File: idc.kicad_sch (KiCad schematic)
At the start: 3 parts, among them Q2401 MMDT5401

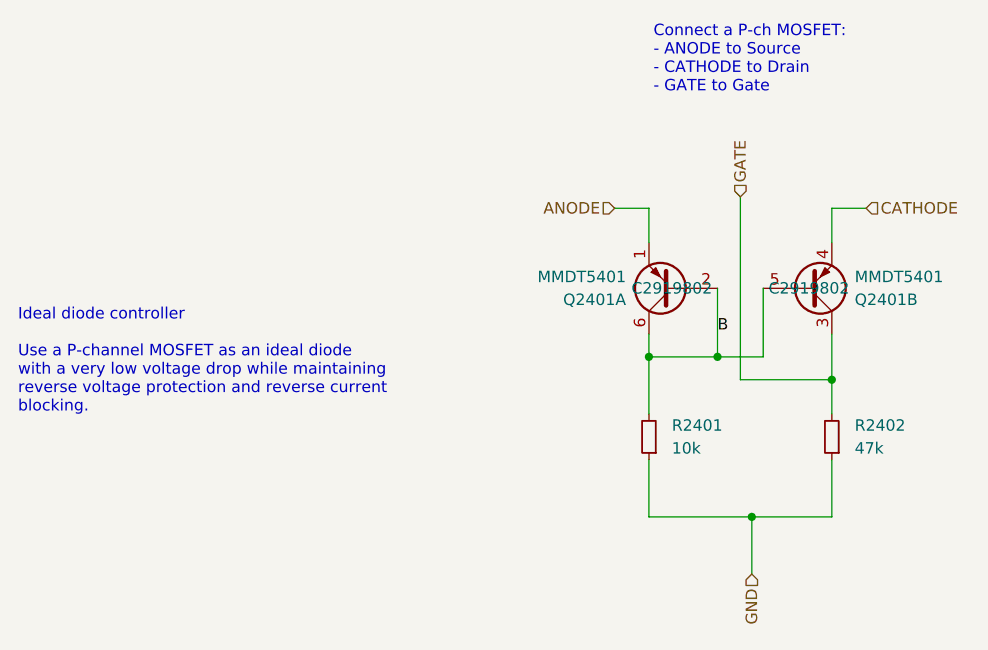
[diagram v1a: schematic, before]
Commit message: Reannotate components
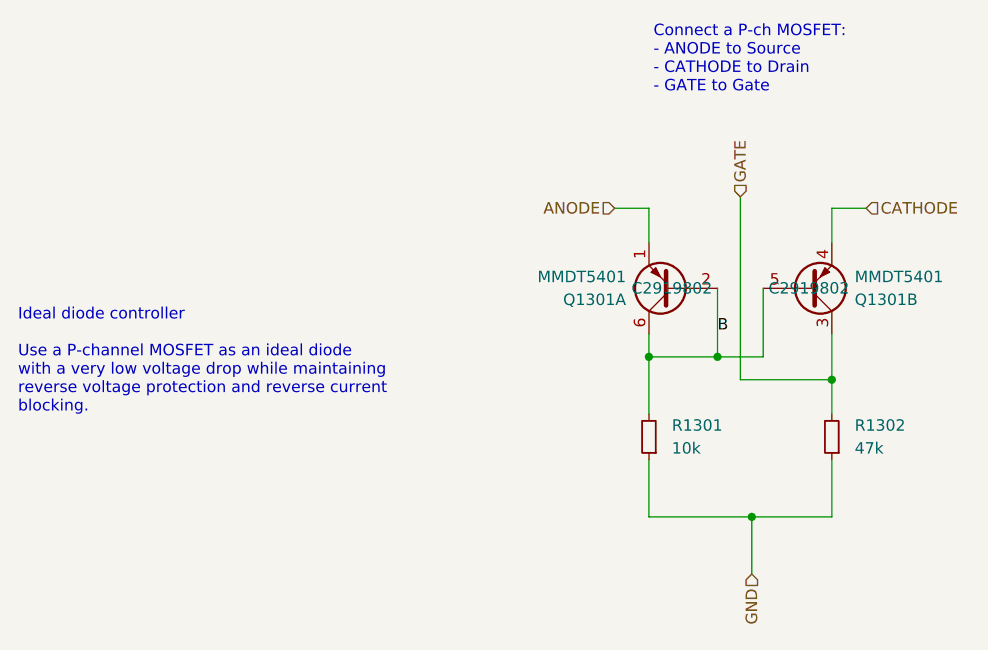
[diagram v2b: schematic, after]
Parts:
- renumbered Q2401 to Q1301, R2401 to R1301, R2402 to R1302
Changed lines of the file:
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@@
 		(dnp no)
 		(fields_autoplaced yes)
-		(property "Reference" "R2402"
+		(property "Reference" "R1302"
 			(at 157.48 107.9499 0)
 			(effects
@@
 			(project "HALPI2"
 				(path "/abc482bd-3f17-4d35-80db-1da3dcdb5c27/850df4bf-e40a-4082-adc2-76804638b949/941fe792-02c8-46de-a01c-95bb6b865738"
-					(reference "R2402")
+					(reference "R1302")
 					(unit 1)
 				)
@@
 		(dnp no)
 		(fields_autoplaced yes)
-		(property "Reference" "R2401"
+		(property "Reference" "R1301"
 			(at 137.16 107.9499 0)
 			(effects
@@
 			(project "HALPI2"
 				(path "/abc482bd-3f17-4d35-80db-1da3dcdb5c27/850df4bf-e40a-4082-adc2-76804638b949/941fe792-02c8-46de-a01c-95bb6b865738"
-					(reference "R2401")
+					(reference "R1301")
 					(unit 1)
 				)
@@
 		(on_board yes)
 		(dnp no)
-		(property "Reference" "Q2401"
+		(property "Reference" "Q1301"
 			(at 157.48 93.9801 0)
 			(effects
@@
 			(project ""
 				(path "/abc482bd-3f17-4d35-80db-1da3dcdb5c27/850df4bf-e40a-4082-adc2-76804638b949/941fe792-02c8-46de-a01c-95bb6b865738"
-					(reference "Q2401")
+					(reference "Q1301")
 					(unit 2)
 				)
@@
 		(on_board yes)
 		(dnp no)
-		(property "Reference" "Q2401"
+		(property "Reference" "Q1301"
 			(at 132.08 93.9801 0)
 			(effects
@@
 			(project ""
 				(path "/abc482bd-3f17-4d35-80db-1da3dcdb5c27/850df4bf-e40a-4082-adc2-76804638b949/941fe792-02c8-46de-a01c-95bb6b865738"
-					(reference "Q2401")
+					(reference "Q1301")
 					(unit 1)
 				)
